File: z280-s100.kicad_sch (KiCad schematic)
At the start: 33 parts, among them J1 S-100 edge connector (100-pin), J2 JTAG header (1x6), J3 Jumper (2-pin header), J4 Jumper (2-pin header), J5 Jumper (2-pin header), J6 Jumper (2-pin header), J7 Jumper (2-pin header), J8 Jumper (2-pin header), U1 Z280 Z-BUS (12 MHz), U10 IS61C5128AS-25 (512Kx8), U11 SST27SF020 (256Kx8), U12 SST27SF020 (256Kx8), U13 MAX232, U14 DS1813, U15 LM7805, U16 74HCT245, U17 74HCT245, U18 74HCT245, U19 74HCT245, U2 ATF1508AS (PLCC-84), U20 74HCT245, U21 74HCT245, U22 IS61C5128AS-25 (512Kx8), U23 IS61C5128AS-25 (512Kx8), U24 ATF1508AS (PLCC-84), U3 74HC573, U4 74HC573, U9 IS61C5128AS-25 (512Kx8), Y1 24 MHz

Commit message: Z280 S-100: 4-layer PCB with power planes and edge-connector test points
gen_pcb.py now emits a 4-layer board (In1.Cu = GND plane, In2.Cu = +5V
plane), imports the S-100 edge connector geometry from the Z80 V3
reference board, and adds a row of test-point vias above each connector
finger. Component reference designators are synced to the schematic's
current annotation (the edge connector is J8). The schematic generator
gained the serial header and symbol text/body layout fixes, and the
schematic, netlist, and PCB were regenerated.

Co-Authored-By: Claude <noreply@anthropic.com>
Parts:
- removed J1: S-100 edge connector (100-pin), Connector_Edge, symbol z280s100:S100_100
- removed J2: JTAG header (1x6), Connector_PinHeader_2.54mm:PinHeader_1x06_P2.54mm_Vertical, symbol z280s100:JTAG
- removed J7, J8: Jumper (2-pin header), Connector_PinHeader_2.54mm:PinHeader_1x02_P2.54mm_Vertical, symbol z280s100:JP
- removed U10, U22, U23: IS61C5128AS-25 (512Kx8), Package_DIP:DIP-32, symbol z280s100:IS61C5128AS
- removed U12: SST27SF020 (256Kx8), Package_DIP:DIP-32, symbol z280s100:SST27SF020
- removed U13: MAX232, Package_DIP:DIP-16, symbol z280s100:MAX232
- removed U14: DS1813, Package_TO_SOT:TO-92, symbol z280s100:DS1813
- removed U15: LM7805, Package_TO_SOT:TO-220-3, symbol z280s100:LM7805
- removed U2: ATF1508AS (PLCC-84), Package_LCC:PLCC-84_THT-Socket, symbol z280s100:ATF1508
- removed U21: 74HCT245, Package_DIP:DIP-20, symbol z280s100:74HCT245
- removed U24: ATF1508AS (PLCC-84), Package_LCC:PLCC-84_THT-Socket, symbol z280s100:ATF1508B
- removed U4: 74HC573, Package_DIP:DIP-20, symbol z280s100:74HC573
- added J1, J2: Jumper (2-pin header), Connector_PinHeader_2.54mm:PinHeader_1x02_P2.54mm_Vertical, symbol z280s100:JP
- added J7: Serial header (2x5), Connector_PinHeader_2.54mm:PinHeader_2x05_P2.54mm_Vertical, symbol z280s100:SERIAL
- added J8: S-100 edge connector (100-pin), Connector_Edge, symbol z280s100:S100_100
- added J9: JTAG header (1x6), Connector_PinHeader_2.54mm:PinHeader_1x06_P2.54mm_Vertical, symbol z280s100:JTAG
- added U10: SST27SF020 (256Kx8), Package_DIP:DIP-32_W15.24mm, symbol z280s100:SST27SF020
- added U12: LM7805, Package_TO_SOT_THT:TO-3, symbol z280s100:LM7805
- added U13: DS1813, Package_TO_SOT:TO-92, symbol z280s100:DS1813
- added U14: MAX232, Package_DIP:DIP-16_W7.62mm, symbol z280s100:MAX232
- added U15: 74HCT245, Package_DIP:DIP-20_W7.62mm, symbol z280s100:74HCT245
- added U2: 74HC573, Package_DIP:DIP-20, symbol z280s100:74HC573
- added U4: ATF1508AS (PLCC-84), Package_LCC:PLCC-84_THT-Socket, symbol z280s100:ATF1508
- added U5: ATF1508AS (PLCC-84), Package_LCC:PLCC-84_THT-Socket, symbol z280s100:ATF1508B
- added U6, U7, U8: IS61C5128AS-25 (512Kx8), Package_DIP:DIP-32_W15.24mm, symbol z280s100:IS61C5128AS
- U11, U9: footprint Package_DIP:DIP-32 -> Package_DIP:DIP-32_W15.24mm
- U16, U17, U18, U19, U20, U3: footprint Package_DIP:DIP-20 -> Package_DIP:DIP-20_W7.62mm
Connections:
- net +16V: now also J8.2 (+16V)
- net +5V: now also J5.2 (B), J6.2 (B), U20.1 (DIR), J1.2 (B), J9.6 (VCC), U12.3 (OUT), U13.3 (VCC), U14.16 (VCC), U15.20 (VCC), U2.20 (VCC), U4.13 (VCCIO), U4.26 (VCCIO), U4.3 (VCCINT), U4.38 (VCCIO), U4.43 (VCCINT), U4.53 (VCCIO), U4.66 (VCCIO), U4.78 (VCCIO), U5.13 (VCCIO), U5.26 (VCCIO), U5.3 (VCCINT), U5.38 (VCCIO), U5.43 (VCCINT), U5.53 (VCCIO), U5.66 (VCCIO), U5.78 (VCCIO), U6.28 (VCC), U7.28 (VCC), U8.28 (VCC); no longer J3.2 (B)
- net +8V: now also J8.1 (+8V), J8.51 (+8V), U12.1 (IN)
- net -16V: now also J8.52 (-16V)
- net A16: now also U17.2 (A0), J2.2 (B), U5.2 (A16), U6.32 (A15), U7.32 (A15), U8.32 (A15); no longer J4.2 (B), U18.2 (A0)
- net A17: now also J3.2 (B), U17.3 (A1), U5.4 (A17), U6.31 (A16), U7.31 (A16), U8.31 (A16); no longer J5.2 (B), U18.3 (A1)
- net A18: now also J4.2 (B), U17.4 (A2), U5.5 (A18), U6.30 (A17), U7.30 (A17), U8.30 (A17); no longer J6.2 (B), U18.4 (A2)
- net A19: now also U17.5 (A3), U5.6 (A19), U6.29 (A18), U7.29 (A18), U8.29 (A18); no longer U18.5 (A3)
- net A20: now also U17.6 (A4), U5.8 (A20); no longer U18.6 (A4)
- net A21: now also U17.7 (A5), U5.9 (A21); no longer U18.7 (A5)
- net A22: now also U17.8 (A6), U5.10 (A22); no longer U18.8 (A6)
- net A23: now also U17.9 (A7), U5.11 (A23); no longer U18.9 (A7)
- net AD0: now also U11.13 (DQ0), U9.11 (DQ0), U2.2 (D0), U5.28 (AD0), U7.11 (DQ0); no longer U3.2 (D0)
- net AD1: now also U11.14 (DQ1), U9.12 (DQ1), U2.3 (D1), U5.29 (AD1), U7.12 (DQ1); no longer U3.3 (D1)
- net AD10: now also U3.4 (D2), U10.15 (DQ2), U5.40 (AD10), U6.13 (DQ2), U8.13 (DQ2); no longer U11.15 (DQ2), U9.13 (DQ2)
- net AD11: now also U3.5 (D3), U10.17 (DQ3), U5.41 (AD11), U6.15 (DQ3), U8.15 (DQ3); no longer U11.17 (DQ3), U9.15 (DQ3)
- net AD12: now also U3.6 (D4), U10.18 (DQ4), U5.44 (AD12), U6.16 (DQ4), U8.16 (DQ4); no longer U11.18 (DQ4), U9.16 (DQ4)
- net AD13: now also U3.7 (D5), U10.19 (DQ5), U5.45 (AD13), U6.17 (DQ5), U8.17 (DQ5); no longer U11.19 (DQ5), U9.17 (DQ5)
- net AD14: now also U3.8 (D6), U10.20 (DQ6), U5.46 (AD14), U6.18 (DQ6), U8.18 (DQ6); no longer U11.20 (DQ6), U9.18 (DQ6)
- net AD15: now also U3.9 (D7), U10.21 (DQ7), U5.48 (AD15), U6.19 (DQ7), U8.19 (DQ7); no longer U11.21 (DQ7), U9.19 (DQ7)
- net AD2: now also U11.15 (DQ2), U9.13 (DQ2), U2.4 (D2), U5.30 (AD2), U7.13 (DQ2); no longer U3.4 (D2)
- net AD3: now also U11.17 (DQ3), U9.15 (DQ3), U2.5 (D3), U5.31 (AD3), U7.15 (DQ3); no longer U3.5 (D3)
- net AD4: now also U11.18 (DQ4), U9.16 (DQ4), U2.6 (D4), U5.33 (AD4), U7.16 (DQ4); no longer U3.6 (D4)
- net AD5: now also U11.19 (DQ5), U9.17 (DQ5), U2.7 (D5), U5.34 (AD5), U7.17 (DQ5); no longer U3.7 (D5)
- net AD6: now also U11.20 (DQ6), U9.18 (DQ6), U2.8 (D6), U5.35 (AD6), U7.18 (DQ6); no longer U3.8 (D6)
- net AD7: now also U11.21 (DQ7), U9.19 (DQ7), U2.9 (D7), U5.36 (AD7), U7.19 (DQ7); no longer U3.9 (D7)
- net AD8: now also U3.2 (D0), U10.13 (DQ0), U5.37 (AD8), U6.11 (DQ0), U8.11 (DQ0); no longer U11.13 (DQ0), U9.11 (DQ0)
- net AD9: now also U3.3 (D1), U10.14 (DQ1), U5.39 (AD9), U6.12 (DQ1), U8.12 (DQ1); no longer U11.14 (DQ1), U9.12 (DQ1)
- net BANK: now also U4.33 (BANK), U5.73 (BANK)
- net BYTE_SEL: now also U15.2 (A0), U4.73 (BYTE_SEL), U5.16 (BYTE_SEL); no longer U16.2 (A0)
- net CPLD_pDBIN: now also U19.4 (A2), U4.51 (CPLD_pDBIN); no longer U20.4 (A2)
- net CPLD_pHLDA: now also U20.2 (A0), U4.54 (CPLD_pHLDA)
- net CPLD_pSTVAL: now also U19.3 (A1), U4.50 (CPLD_pSTVAL); no longer U20.3 (A1)
- net CPLD_pSYNC: now also U19.2 (A0), U4.49 (CPLD_pSYNC); no longer U20.2 (A0)
- net CPLD_pWR: now also U19.5 (A3), U4.52 (CPLD_pWR); no longer U20.5 (A3)
- net CPLD_sHLTA: now also U18.7 (A5), U4.46 (CPLD_sHLTA); no longer U19.7 (A5)
- net CPLD_sINP: now also U18.4 (A2), U4.41 (CPLD_sINP); no longer U19.4 (A2)
- net CPLD_sINTA: now also U18.6 (A4), U4.45 (CPLD_sINTA); no longer U19.6 (A4)
- net CPLD_sMEMR: now also U18.2 (A0), U4.39 (CPLD_sMEMR); no longer U19.2 (A0)
- net CPLD_sOUT: now also U18.5 (A3), U4.44 (CPLD_sOUT); no longer U19.5 (A3)
- net CPLD_sWO: now also U18.3 (A1), U4.40 (CPLD_sWO); no longer U19.3 (A1)
- net CPLD_sXTRQ: now also U18.8 (A6), U4.48 (CPLD_sXTRQ); no longer U19.8 (A6)
- net FLASH_A15: now also J2.1 (A), U10.3 (A15); no longer J4.1 (A)
- net FLASH_A16: now also J3.1 (A), U10.2 (A16); no longer J5.1 (A)
- net FLASH_A17: now also J4.1 (A), U10.30 (A17); no longer J6.1 (A)
- net FLASH_CE: now also U10.22 (CE), U4.61 (FLASH_CE)
- net FLASH_OE: now also U10.24 (OE), U4.63 (FLASH_OE)
- net FLASH_PGM: now also J5.1 (A), U10.31 (PGM)
- net FLASH_VDD: now also J6.1 (A), U10.32 (VCC)
- net FLASH_VPP: now also J1.1 (A), U10.1 (VPP); no longer J3.1 (A)
- net FLASH_WIN: now also U4.31 (FLASH_WIN), U5.70 (FLASH_WIN)
- net GND: now also U20.19 (OE), U20.3 (A1), U20.4 (A2), U20.5 (A3), U20.6 (A4), U20.7 (A5), U20.8 (A6), U20.9 (A7), J7.10 (GND), J7.3 (GND), J7.4 (GND), J7.5 (GND), J7.6 (GND), J7.7 (GND), J7.8 (GND), J7.9 (GND), J8.100 (GND), J8.20 (GND), J8.50 (GND), J8.53 (GND), J8.70 (GND), J9.5 (GND), U10.16 (GND), U12.2 (GND), U13.1 (GND), U14.15 (GND), U15.10 (GND), U2.1 (OE), U2.10 (GND), U4.19 (GND), U4.32 (GND), U4.42 (GND), U4.47 (GND), U4.59 (GND), U4.7 (GND), U4.72 (GND), U4.82 (GND), U5.19 (GND), U5.32 (GND), U5.42 (GND), U5.47 (GND), U5.59 (GND), U5.7 (GND), U5.72 (GND), U5.82 (GND), U6.14 (GND), U7.14 (GND), U8.14 (GND)
- net JTAG_CHAIN: now also U4.71 (TDO), U5.14 (TDI)
- net JTAG_TCK: now also J9.1 (TCK), U4.62 (TCK), U5.62 (TCK)
- net JTAG_TDI: now also J9.3 (TDI), U4.14 (TDI)
- net JTAG_TDO: now also J9.4 (TDO), U5.71 (TDO)
- net JTAG_TMS: now also J9.2 (TMS), U4.23 (TMS), U5.23 (TMS)
- net LA0: now also U2.12 (Q0), U4.27 (LA0); no longer U3.12 (Q0)
- net LA1: now also U10.12 (A0), U15.3 (A1), U2.13 (Q1), U4.28 (LA1); no longer U16.3 (A1), U3.13 (Q1)
- net LA10: now also U16.4 (A2), U3.14 (Q2), U10.26 (A9), U6.24 (A9), U7.24 (A9), U8.24 (A9); no longer U17.4 (A2)
- net LA11: now also U16.5 (A3), U3.15 (Q3), U10.23 (A10), U6.21 (A10), U7.21 (A10), U8.21 (A10); no longer U17.5 (A3)
- net LA12: now also U16.6 (A4), U3.16 (Q4), U10.25 (A11), U6.23 (A11), U7.23 (A11), U8.23 (A11); no longer U17.6 (A4)
- net LA13: now also U16.7 (A5), U3.17 (Q5), U10.4 (A12), U6.2 (A12), U7.2 (A12), U8.2 (A12); no longer U17.7 (A5)
- net LA14: now also U16.8 (A6), U3.18 (Q6), U10.28 (A13), U6.26 (A13), U7.26 (A13), U8.26 (A13); no longer U17.8 (A6)
- net LA15: now also U16.9 (A7), U3.19 (Q7), U10.29 (A14), U6.1 (A14), U7.1 (A14), U8.1 (A14); no longer U17.9 (A7)
- net LA2: now also U10.11 (A1), U15.4 (A2), U2.14 (Q2), U4.29 (LA2); no longer U16.4 (A2), U3.14 (Q2)
- net LA3: now also U10.10 (A2), U15.5 (A3), U2.15 (Q3), U6.8 (A2), U7.8 (A2), U8.8 (A2); no longer U16.5 (A3), U3.15 (Q3)
- net LA4: now also U10.9 (A3), U15.6 (A4), U2.16 (Q4), U6.7 (A3), U7.7 (A3), U8.7 (A3); no longer U16.6 (A4), U3.16 (Q4)
- net LA5: now also U10.8 (A4), U15.7 (A5), U2.17 (Q5), U6.6 (A4), U7.6 (A4), U8.6 (A4); no longer U16.7 (A5), U3.17 (Q5)
- net LA6: now also U10.7 (A5), U15.8 (A6), U2.18 (Q6), U6.5 (A5), U7.5 (A5), U8.5 (A5); no longer U16.8 (A6), U3.18 (Q6)
- net LA7: now also U10.6 (A6), U15.9 (A7), U2.19 (Q7), U6.4 (A6), U7.4 (A6), U8.4 (A6); no longer U16.9 (A7), U3.19 (Q7)
- net LA8: now also U16.2 (A0), U3.12 (Q0), U10.5 (A7), U6.3 (A7), U7.3 (A7), U8.3 (A7); no longer U17.2 (A0)
- net LA9: now also U16.3 (A1), U3.13 (Q1), U10.27 (A8), U6.25 (A8), U7.25 (A8), U8.25 (A8); no longer U17.3 (A1)
- net LATCH_LE: now also U2.11 (LE), U4.64 (LATCH_LE)
- net MASTER_ACTIVE: now also U4.69 (MASTER_ACTIVE), U5.12 (MASTER_ACTIVE)
- net MASTER_WRITE: now also U4.70 (MASTER_WRITE), U5.15 (MASTER_WRITE)
- net MAX_C1M: now also U14.3 (C1-)
- net MAX_C1P: now also U14.1 (C1+)
- net MAX_C2M: now also U14.5 (C2-)
- net MAX_C2P: now also U14.4 (C2+)
- net MAX_RS232_TX: now also J7.1 (RS232_TX), U14.14 (T1OUT)
- net MAX_VM: now also U14.6 (V-)
- net MAX_VP: now also U14.2 (V+)
- net MEM_CE0: now also U4.55 (MEM_CE0), U6.20 (CE), U7.20 (CE); no longer U9.20 (CE)
- net MEM_CE1: now also U9.20 (CE), U4.56 (MEM_CE1), U8.20 (CE)
- net MEM_OE: now also U4.57 (MEM_OE), U6.22 (OE), U7.22 (OE), U8.22 (OE)
- net MEM_WE_H: now also U9.27 (WE), U4.60 (MEM_WE_H), U7.27 (WE)
- net MEM_WE_L: now also U4.58 (MEM_WE_L), U6.27 (WE), U8.27 (WE); no longer U9.27 (WE)
- net NC: now also U14.10 (T2IN), U14.7 (T2OUT), U14.8 (R2IN), U14.9 (R2OUT)
- net S100_A0: now also J8.79 (A0), U15.11 (B0); no longer U16.11 (B0)
- net S100_A1: now also J8.80 (A1), U15.12 (B1); no longer U16.12 (B1)
- net S100_A10: now also U16.13 (B2), J8.37 (A10); no longer U17.13 (B2)
- net S100_A11: now also U16.14 (B3), J8.87 (A11); no longer U17.14 (B3)
- net S100_A12: now also U16.15 (B4), J8.33 (A12); no longer U17.15 (B4)
- net S100_A13: now also U16.16 (B5), J8.85 (A13); no longer U17.16 (B5)
- net S100_A14: now also U16.17 (B6), J8.86 (A14); no longer U17.17 (B6)
- net S100_A15: now also U16.18 (B7), J8.32 (A15); no longer U17.18 (B7)
- net S100_A16: now also U17.11 (B0), J8.16 (A16); no longer U18.11 (B0)
- net S100_A17: now also U17.12 (B1), J8.17 (A17); no longer U18.12 (B1)
- net S100_A18: now also U17.13 (B2), J8.15 (A18); no longer U18.13 (B2)
- net S100_A19: now also U17.14 (B3), J8.59 (A19); no longer U18.14 (B3)
- net S100_A2: now also J8.81 (A2), U15.13 (B2); no longer U16.13 (B2)
- net S100_A20: now also U17.15 (B4), J8.61 (A20); no longer U18.15 (B4)
- net S100_A21: now also U17.16 (B5), J8.62 (A21); no longer U18.16 (B5)
- net S100_A22: now also U17.17 (B6), J8.63 (A22); no longer U18.17 (B6)
- net S100_A23: now also U17.18 (B7), J8.64 (A23); no longer U18.18 (B7)
- net S100_A3: now also J8.31 (A3), U15.14 (B3); no longer U16.14 (B3)
- net S100_A4: now also J8.30 (A4), U15.15 (B4); no longer U16.15 (B4)
- net S100_A5: now also J8.29 (A5), U15.16 (B5); no longer U16.16 (B5)
- net S100_A6: now also J8.82 (A6), U15.17 (B6); no longer U16.17 (B6)
- net S100_A7: now also J8.83 (A7), U15.18 (B7); no longer U16.18 (B7)
- net S100_A8: now also U16.11 (B0), J8.84 (A8); no longer U17.11 (B0)
- net S100_A9: now also U16.12 (B1), J8.34 (A9); no longer U17.12 (B1)
- net S100_ADSB: now also J8.22 (ADSB), U5.22 (S100_ADSB)
- net S100_A_DIR: now also U15.1 (DIR), U5.75 (S100_A_DIR); no longer U18.1 (DIR)
- net S100_A_OE: now also U15.19 (OE), U5.74 (S100_A_OE); no longer U18.19 (OE)
- net S100_CDSB: now also J8.19 (CDSB), U5.27 (S100_CDSB)
- net S100_CLOCK: now also J8.49 (CLOCK)
- net S100_C_OE: now also U19.19 (OE), U5.77 (S100_C_OE); no longer U20.19 (OE)
- net S100_DI0: now also J8.95 (DI0), U5.58 (S100_DI0)
- net S100_DI1: now also J8.94 (DI1), U5.60 (S100_DI1)
- net S100_DI2: now also J8.41 (DI2), U5.61 (S100_DI2)
- net S100_DI3: now also J8.42 (DI3), U5.63 (S100_DI3)
- net S100_DI4: now also J8.91 (DI4), U5.64 (S100_DI4)
- net S100_DI5: now also J8.92 (DI5), U5.65 (S100_DI5)
- net S100_DI6: now also J8.93 (DI6), U5.67 (S100_DI6)
- net S100_DI7: now also J8.43 (DI7), U5.68 (S100_DI7)
- net S100_DMA0: now also J8.55 (DMA0)
- net S100_DMA1: now also J8.56 (DMA1)
- net S100_DMA2: now also J8.57 (DMA2)
- net S100_DMA3: now also J8.14 (DMA3)
- net S100_DO0: now also J8.36 (DO0), U5.49 (S100_DO0)
- net S100_DO1: now also J8.35 (DO1), U5.50 (S100_DO1)
- net S100_DO2: now also J8.88 (DO2), U5.51 (S100_DO2)
- net S100_DO3: now also J8.89 (DO3), U5.52 (S100_DO3)
- net S100_DO4: now also J8.38 (DO4), U5.54 (S100_DO4)
- net S100_DO5: now also J8.39 (DO5), U5.55 (S100_DO5)
- net S100_DO6: now also J8.40 (DO6), U5.56 (S100_DO6)
- net S100_DO7: now also J8.90 (DO7), U5.57 (S100_DO7)
- net S100_DODSB: now also J8.23 (DODSB), U5.24 (S100_DODSB)
- net S100_ERROR: now also J8.98 (ERROR)
- net S100_HOLD: now also J8.74 (HOLD), U4.20 (S100_HOLD)
- net S100_INT: now also J8.73 (INT), U4.17 (S100_INT)
- net S100_MWRT: now also J8.68 (MWRT)
- net S100_NMI: now also J8.12 (NMI), U4.18 (S100_NMI)
- net S100_PHANTOM: now also J8.67 (PHANTOM)
- net S100_PHI: now also J8.24 (PHI)
- net S100_POC: now also J8.99 (POC)
- net S100_PWRFAIL: now also J8.13 (PWRFAIL)
- net S100_RESET: now also J8.75 (RESET)
- net S100_SC_DIR: now also U18.1 (DIR), U5.79 (S100_SC_DIR); no longer U20.1 (DIR)
- net S100_SDSB: now also J8.18 (SDSB), U5.25 (S100_SDSB)
- net S100_SIXTN: now also J8.60 (SIXTN), U4.24 (S100_SIXTN), U5.83 (S100_SIXTN)
- net S100_SLAVE_CLR: now also J8.54 (SLAVE_CLR)
- net S100_S_OE: now also U18.19 (OE), U5.76 (S100_S_OE); no longer U19.19 (OE)
- net S100_VI0: now also J8.4 (VI0)
- net S100_VI1: now also J8.5 (VI1)
- net S100_VI2: now also J8.6 (VI2)
- net S100_VI3: now also J8.7 (VI3)
- net S100_VI4: now also J8.8 (VI4)
- net S100_VI5: now also J8.9 (VI5)
- net S100_VI6: now also J8.10 (VI6)
- net S100_VI7: now also J8.11 (VI7)
- net S100_XRDY: now also J8.3 (XRDY), U4.22 (S100_XRDY), U5.81 (S100_XRDY)
- net S100_pDBIN: now also U19.13 (B2), J8.78 (pDBIN); no longer U20.13 (B2)
- net S100_pHLDA: now also U20.11 (B0), J8.26 (pHLDA)
- net S100_pRDY: now also J8.72 (pRDY), U4.21 (S100_pRDY), U5.80 (S100_pRDY)
- net S100_pSTVAL: now also U19.12 (B1), J8.25 (pSTVAL); no longer U20.12 (B1)
- net S100_pSYNC: now also U19.11 (B0), J8.76 (pSYNC); no longer U20.11 (B0)
- net S100_pWR: now also U19.14 (B3), J8.77 (pWR); no longer U20.14 (B3)
- net S100_sHLTA: now also U18.16 (B5), J8.48 (sHLTA); no longer U19.16 (B5)
- net S100_sINP: now also U18.13 (B2), J8.46 (sINP); no longer U19.13 (B2)
- net S100_sINTA: now also U18.15 (B4), J8.96 (sINTA); no longer U19.15 (B4)
- net S100_sM1: now also J8.44 (sM1)
- net S100_sMEMR: now also U18.11 (B0), J8.47 (sMEMR), U5.18 (S100_sMEMR); no longer U19.11 (B0)
- net S100_sOUT: now also U18.14 (B3), J8.45 (sOUT); no longer U19.14 (B3)
- net S100_sWO: now also U18.12 (B1), J8.97 (sWO), U5.20 (S100_sWO); no longer U19.12 (B1)
- net S100_sXTRQ: now also U18.17 (B6), J8.58 (sXTRQ), U5.21 (S100_sXTRQ); no longer U19.17 (B6)
- net SLAVE: now also U4.68 (SLAVE), U5.1 (SLAVE)
- net SLAVE_ONLY: now also U4.25 (SLAVE_ONLY)
- net SRAM_A0: now also U4.65 (SRAM_A0), U6.10 (A0), U7.10 (A0), U8.10 (A0)
- net SRAM_A1: now also U4.67 (SRAM_A1), U6.9 (A1), U7.9 (A1), U8.9 (A1)
- net SRAM_WIN: now also U4.30 (SRAM_WIN), U5.69 (SRAM_WIN)
- net XFR16: now also U4.74 (XFR16), U5.17 (XFR16)
- net Z_AS: now also U4.1 (Z_AS)
- net Z_BUSACK: now also U4.15 (Z_BUSACK)
- net Z_BUSREQ: now also U4.37 (Z_BUSREQ)
- net Z_BW: now also U4.5 (Z_BW)
- net Z_CLK: now also U4.83 (Z_CLK_IN)
- net Z_DS: now also U4.2 (Z_DS)
- net Z_IE: now also U4.11 (Z_IE)
- net Z_INT: now also U4.35 (Z_INT)
- net Z_NMI: now also U4.36 (Z_NMI)
- net Z_OE: now also U4.12 (Z_OE)
- net Z_RESET: now also U13.2 (RST), U4.16 (Z_RESET)
- net Z_RW: now also U4.4 (Z_RW)
- net Z_RXD: now also U14.12 (R1OUT)
- net Z_ST0: now also U4.6 (Z_ST0)
- net Z_ST1: now also U4.8 (Z_ST1)
- net Z_ST2: now also U4.9 (Z_ST2)
- net Z_ST3: now also U4.10 (Z_ST3)
- net Z_TXD: now also U14.11 (T1IN)
- net Z_WAIT: now also U4.34 (Z_WAIT)
- new net MAX_RS232_RX: J7.2 (RS232_RX), U14.13 (R1IN)

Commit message: Z280 S-100: re-partition CPLDs, external decode, reset/BTI config
Split the two ATF1508s by function: z280-s100-ad.pld (data path) owns
AD0-15 demux/burst/byte-mux, z280-s100-ctl.pld (decider) owns the FSM,
arbitration, memory control and steering. Replace the old
control.pld/data.pld pair.

Move A16-23 decode off-chip to a 74F138 + two 74F521s (SRAM/FLASH/slave
window); drop the 74HC573 latches. Boot ROM is now 2x AT28C256 (word-wide
fetch needs two parts).

Add reset/BTI loading: a 74HCT244 tri-state driver (CFG_OE-gated) drives
AD0-7 during reset, config jumpers J10-J17 strap the BTI value, and a
15-clock hold counter keeps WAIT asserted past reset. Fix dedicated pins
(GCLR/OE1/OE2 tied inactive) and make SIXTN bidirectional.

PCB: RAM/ROM clustered left, decode + BTI + config straps top-right,
data CPLD aligned above the memory column.

Co-Authored-By: Claude <noreply@anthropic.com>
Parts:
- removed J1, J2, J3, J4, J5, J6: Jumper (2-pin header), Connector_PinHeader_2.54mm:PinHeader_1x02_P2.54mm_Vertical, symbol z280s100:JP
- removed U10, U11: SST27SF020 (256Kx8), Package_DIP:DIP-32_W15.24mm, symbol z280s100:SST27SF020
- removed U2: 74HC573, Package_DIP:DIP-20, symbol z280s100:74HC573
- removed U3: 74HC573, Package_DIP:DIP-20_W7.62mm, symbol z280s100:74HC573
- added J10, J11, J12, J13, J14, J15, J16, J17: Jumper (3-pin header), Connector_PinHeader_2.54mm:PinHeader_1x03_P2.54mm_Vertical, symbol z280s100:JP3
- added U10, U11: AT28C256 (32Kx8), Package_DIP:DIP-28_W15.24mm, symbol z280s100:AT28C256
- added U21: 74HCT244, Package_DIP:DIP-20, symbol z280s100:74HCT244
- added U22: 74F138, Package_DIP:DIP-16, symbol z280s100:74F138
- added U23, U24: 74F521, Package_DIP:DIP-20, symbol z280s100:74F521
- U12: footprint Package_TO_SOT_THT:TO-3 -> Package_TO_SOT:TO-220-3
- U14: footprint Package_DIP:DIP-16_W7.62mm -> Package_DIP:DIP-16
- U15, U16, U17, U18, U19, U20: footprint Package_DIP:DIP-20_W7.62mm -> Package_DIP:DIP-20
- U6, U7, U8, U9: footprint Package_DIP:DIP-32_W15.24mm -> Package_DIP:DIP-32
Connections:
- net LATCH_LE is gone; now on net S100_A_OE: U4.64 (S100_A_OE)
- net +5V: now also U4.1 (GCLR), U4.2 (OE2), U4.84 (OE1), U5.1 (GCLR), U5.2 (OE2), U5.84 (OE1), J10.1 (HIGH), J11.1 (HIGH), J12.1 (HIGH), J13.1 (HIGH), J14.1 (HIGH), J15.1 (HIGH), J16.1 (HIGH), J17.1 (HIGH), U10.28 (VCC), U11.28 (VCC), U21.20 (+5V), U22.16 (+5V), U22.6 (G1), U23.12 (P4), U23.14 (P5), U23.16 (P6), U23.18 (P7), U23.20 (+5V), U24.20 (+5V)
- net A16: now also U23.3 (Q0), U24.2 (P0), U24.3 (Q0); no longer U5.2 (A16)
- net A17: now also U23.5 (Q1), U24.4 (P1), U24.5 (Q1); no longer U5.4 (A17)
- net A18: now also U23.7 (Q2), U24.6 (P2), U24.7 (Q2); no longer U5.5 (A18)
- net A19: now also U23.9 (Q3), U24.8 (P3), U24.9 (Q3); no longer U5.6 (A19)
- net A20: now also U23.11 (Q4), U24.11 (Q4), U24.12 (P4); no longer U5.8 (A20)
- net A21: now also U22.1 (A0), U23.13 (Q5), U24.13 (Q5); no longer U5.9 (A21)
- net A22: now also U22.2 (A1), U23.15 (Q6), U24.15 (Q6); no longer U5.10 (A22)
- net A23: now also U22.3 (A2), U23.17 (Q7), U24.17 (Q7); no longer U5.11 (A23)
- net AD0: now also U5.40 (AD0), U11.11 (DQ0), U21.18 (Y0); no longer U5.28 (AD0)
- net AD1: now also U5.41 (AD1), U11.12 (DQ1), U21.16 (Y1); no longer U5.29 (AD1)
- net AD10: now also U5.54 (AD10), U10.13 (DQ2); no longer U5.40 (AD10)
- net AD11: now also U5.55 (AD11), U10.15 (DQ3); no longer U5.41 (AD11)
- net AD12: now also U5.56 (AD12), U10.16 (DQ4); no longer U5.44 (AD12)
- net AD13: now also U5.57 (AD13), U10.17 (DQ5); no longer U5.45 (AD13)
- net AD14: now also U5.58 (AD14), U10.18 (DQ6); no longer U5.46 (AD14)
- net AD15: now also U5.60 (AD15), U10.19 (DQ7); no longer U5.48 (AD15)
- net AD2: now also U5.44 (AD2), U11.13 (DQ2), U21.14 (Y2); no longer U5.30 (AD2)
- net AD3: now also U5.45 (AD3), U11.15 (DQ3), U21.12 (Y3); no longer U5.31 (AD3)
- net AD4: now also U5.46 (AD4), U11.16 (DQ4), U21.9 (Y4); no longer U5.33 (AD4)
- net AD5: now also U5.48 (AD5), U11.17 (DQ5), U21.7 (Y5); no longer U5.34 (AD5)
- net AD6: now also U5.49 (AD6), U11.18 (DQ6), U21.5 (Y6); no longer U5.35 (AD6)
- net AD7: now also U5.50 (AD7), U11.19 (DQ7), U21.3 (Y7); no longer U5.36 (AD7)
- net AD8: now also U5.51 (AD8), U10.11 (DQ0); no longer U5.37 (AD8)
- net AD9: now also U5.52 (AD9), U10.12 (DQ1); no longer U5.39 (AD9)
- net BANK: no longer U5.73 (BANK)
- net FLASH_CE: now also U10.20 (CE), U11.20 (CE)
- net FLASH_OE: now also U10.22 (OE), U11.22 (OE)
- net FLASH_WIN: now also U23.19 (PEQQ); no longer U5.70 (FLASH_WIN)
- net GND: now also J10.3 (LOW), J11.3 (LOW), J12.3 (LOW), J13.3 (LOW), J14.3 (LOW), J15.3 (LOW), J16.3 (LOW), J17.3 (LOW), U10.14 (GND), U11.14 (GND), U21.10 (GND), U22.4 (G2A), U22.5 (G2B), U22.8 (GND), U23.1 (G), U23.10 (GND), U23.2 (P0), U23.4 (P1), U23.6 (P2), U23.8 (P3), U24.1 (G), U24.10 (GND), U24.14 (P5), U24.16 (P6), U24.18 (P7)
- net LA0: now also U5.18 (LA0)
- net LA1: no longer U4.28 (LA1)
- net LA10: no longer U6.24 (A9), U7.24 (A9), U8.24 (A9), U9.24 (A9)
- net LA11: no longer U6.21 (A10), U7.21 (A10), U8.21 (A10), U9.21 (A10)
- net LA12: no longer U6.23 (A11), U7.23 (A11), U8.23 (A11), U9.23 (A11)
- net LA13: no longer U6.2 (A12), U7.2 (A12), U8.2 (A12), U9.2 (A12)
- net LA14: no longer U6.26 (A13), U7.26 (A13), U8.26 (A13), U9.26 (A13)
- net LA15: no longer U6.1 (A14), U7.1 (A14), U8.1 (A14), U9.1 (A14)
- net LA2: no longer U4.29 (LA2)
- net LA3: no longer U6.8 (A2), U7.8 (A2), U8.8 (A2), U9.8 (A2)
- net LA4: no longer U6.7 (A3), U7.7 (A3), U8.7 (A3), U9.7 (A3)
- net LA5: no longer U6.6 (A4), U7.6 (A4), U8.6 (A4), U9.6 (A4)
- net LA6: no longer U6.5 (A5), U7.5 (A5), U8.5 (A5), U9.5 (A5)
- net LA7: no longer U6.4 (A6), U7.4 (A6), U8.4 (A6), U9.4 (A6)
- net LA8: no longer U6.3 (A7), U7.3 (A7), U8.3 (A7), U9.3 (A7)
- net LA9: no longer U6.25 (A8), U7.25 (A8), U8.25 (A8), U9.25 (A8)
- net S100_ADSB: now also U4.12 (S100_ADSB); no longer U5.22 (S100_ADSB)
- net S100_A_OE: no longer U5.74 (S100_A_OE)
- net S100_CDSB: now also U4.28 (S100_CDSB); no longer U5.27 (S100_CDSB)
- net S100_C_OE: now also U4.67 (S100_C_OE); no longer U5.77 (S100_C_OE)
- net S100_DI0: now also U5.73 (S100_DI0); no longer U5.58 (S100_DI0)
- net S100_DI1: now also U5.74 (S100_DI1); no longer U5.60 (S100_DI1)
- net S100_DI2: now also U5.75 (S100_DI2); no longer U5.61 (S100_DI2)
- net S100_DI3: now also U5.76 (S100_DI3); no longer U5.63 (S100_DI3)
- net S100_DI4: now also U5.77 (S100_DI4); no longer U5.64 (S100_DI4)
- net S100_DI5: now also U5.79 (S100_DI5); no longer U5.65 (S100_DI5)
- net S100_DI6: now also U5.80 (S100_DI6); no longer U5.67 (S100_DI6)
- net S100_DI7: now also U5.81 (S100_DI7); no longer U5.68 (S100_DI7)
- net S100_DO0: now also U5.61 (S100_DO0); no longer U5.49 (S100_DO0)
- net S100_DO1: now also U5.63 (S100_DO1); no longer U5.50 (S100_DO1)
- net S100_DO2: now also U5.64 (S100_DO2); no longer U5.51 (S100_DO2)
- net S100_DO3: now also U5.65 (S100_DO3); no longer U5.52 (S100_DO3)
- net S100_DO4: now also U5.67 (S100_DO4); no longer U5.54 (S100_DO4)
- net S100_DO5: now also U5.68 (S100_DO5); no longer U5.55 (S100_DO5)
- net S100_DO6: now also U5.69 (S100_DO6); no longer U5.56 (S100_DO6)
- net S100_DO7: now also U5.70 (S100_DO7); no longer U5.57 (S100_DO7)
- net S100_DODSB: now also U5.8 (S100_DODSB); no longer U5.24 (S100_DODSB)
- net S100_SDSB: now also U4.25 (S100_SDSB); no longer U5.25 (S100_SDSB)
- net S100_SIXTN: no longer U5.83 (S100_SIXTN)
- net S100_S_OE: now also U4.65 (S100_S_OE); no longer U5.76 (S100_S_OE)
- net S100_XRDY: no longer U5.81 (S100_XRDY)
- net S100_pRDY: no longer U5.80 (S100_pRDY)
- net S100_sMEMR: no longer U5.18 (S100_sMEMR)
- net S100_sWO: no longer U5.20 (S100_sWO)
- net S100_sXTRQ: no longer U5.21 (S100_sXTRQ)
- net SLAVE: now also U5.17 (SLAVE); no longer U5.1 (SLAVE)
- net SLAVE_ONLY: no longer U4.25 (SLAVE_ONLY)
- net SRAM_WIN: now also U22.15 (Y0); no longer U5.69 (SRAM_WIN)
- net XFR16: now also U5.15 (XFR16); no longer U5.17 (XFR16)
- net Z_AS: now also U4.77 (Z_AS), U5.4 (Z_AS); no longer U4.1 (Z_AS)
- net Z_CLK: now also U5.83 (Z_CLK_IN)
- net Z_DS: now also U4.79 (Z_DS), U5.5 (Z_DS); no longer U4.2 (Z_DS)
- net Z_OE: no longer U4.12 (Z_OE)
- net BYTE_SEL renamed SPLIT
- net SPLIT: no longer U15.2 (A0)
- net MASTER_ACTIVE renamed MST_RD
- net MST_RD: now also U5.9 (MST_RD); no longer U5.12 (MASTER_ACTIVE)
- net MASTER_WRITE renamed MST_WR
- net MST_WR: now also U5.10 (MST_WR); no longer U5.15 (MASTER_WRITE)
- net S100_A_DIR renamed S100_DIR
- net S100_DIR: now also U18.1 (DIR), U19.1 (DIR), U5.6 (S100_DIR); no longer U5.75 (S100_A_DIR)
- removed net S100_SC_DIR: U18.1 (DIR), U19.1 (DIR), U5.79 (S100_SC_DIR)
- net SRAM_A0 renamed A1
- net A1: now also U5.21 (A1), U10.10 (A0), U11.10 (A0); no longer U4.65 (SRAM_A0)
- net SRAM_A1 renamed A2
- net A2: now also U5.22 (A2), U10.9 (A1), U11.9 (A1); no longer U4.67 (SRAM_A1)
- new net A0: U15.2 (A0), U5.20 (A0)
- new net A10: U10.24 (A9), U11.24 (A9), U5.33 (A10), U6.24 (A9), U7.24 (A9), U8.24 (A9), U9.24 (A9)
- new net A11: U10.21 (A10), U11.21 (A10), U5.34 (A11), U6.21 (A10), U7.21 (A10), U8.21 (A10), U9.21 (A10)
- new net A12: U10.23 (A11), U11.23 (A11), U5.35 (A12), U6.23 (A11), U7.23 (A11), U8.23 (A11), U9.23 (A11)
- new net A13: U10.2 (A12), U11.2 (A12), U5.36 (A13), U6.2 (A12), U7.2 (A12), U8.2 (A12), U9.2 (A12)
- new net A14: U10.26 (A13), U11.26 (A13), U5.37 (A14), U6.26 (A13), U7.26 (A13), U8.26 (A13), U9.26 (A13)
- new net A15: U10.1 (A14), U11.1 (A14), U5.39 (A15), U6.1 (A14), U7.1 (A14), U8.1 (A14), U9.1 (A14)
- new net A3: U10.8 (A2), U11.8 (A2), U5.24 (A3), U6.8 (A2), U7.8 (A2), U8.8 (A2), U9.8 (A2)
- new net A4: U10.7 (A3), U11.7 (A3), U5.25 (A4), U6.7 (A3), U7.7 (A3), U8.7 (A3), U9.7 (A3)
- new net A5: U10.6 (A4), U11.6 (A4), U5.27 (A5), U6.6 (A4), U7.6 (A4), U8.6 (A4), U9.6 (A4)
- new net A6: U10.5 (A5), U11.5 (A5), U5.28 (A6), U6.5 (A5), U7.5 (A5), U8.5 (A5), U9.5 (A5)
- new net A7: U10.4 (A6), U11.4 (A6), U5.29 (A7), U6.4 (A6), U7.4 (A6), U8.4 (A6), U9.4 (A6)
- new net A8: U10.3 (A7), U11.3 (A7), U5.30 (A8), U6.3 (A7), U7.3 (A7), U8.3 (A7), U9.3 (A7)
- new net A9: U10.25 (A8), U11.25 (A8), U5.31 (A9), U6.25 (A8), U7.25 (A8), U8.25 (A8), U9.25 (A8)
- new net BTI_AD0: J10.2 (SEL), U21.2 (A0)
- new net BTI_AD1: J11.2 (SEL), U21.4 (A1)
- new net BTI_AD2: J12.2 (SEL), U21.6 (A2)
- new net BTI_AD3: J13.2 (SEL), U21.8 (A3)
- new net BTI_AD4: J14.2 (SEL), U21.11 (A4)
- new net BTI_AD5: J15.2 (SEL), U21.13 (A5)
- new net BTI_AD6: J16.2 (SEL), U21.15 (A6)
- new net BTI_AD7: J17.2 (SEL), U21.17 (A7)
- new net CFG_OE: U21.1 (OE1), U21.19 (OE2), U4.75 (CFG_OE)
- new net FLASH_WE: U10.27 (WE), U11.27 (WE), U4.76 (FLASH_WE)
- new net SLAVE_WIN: U24.19 (PEQQ), U4.29 (SLAVE_WIN)
- new net SLV_RD: U4.80 (SLV_RD), U5.11 (SLV_RD)
- new net SLV_WR: U4.81 (SLV_WR), U5.12 (SLV_WR)

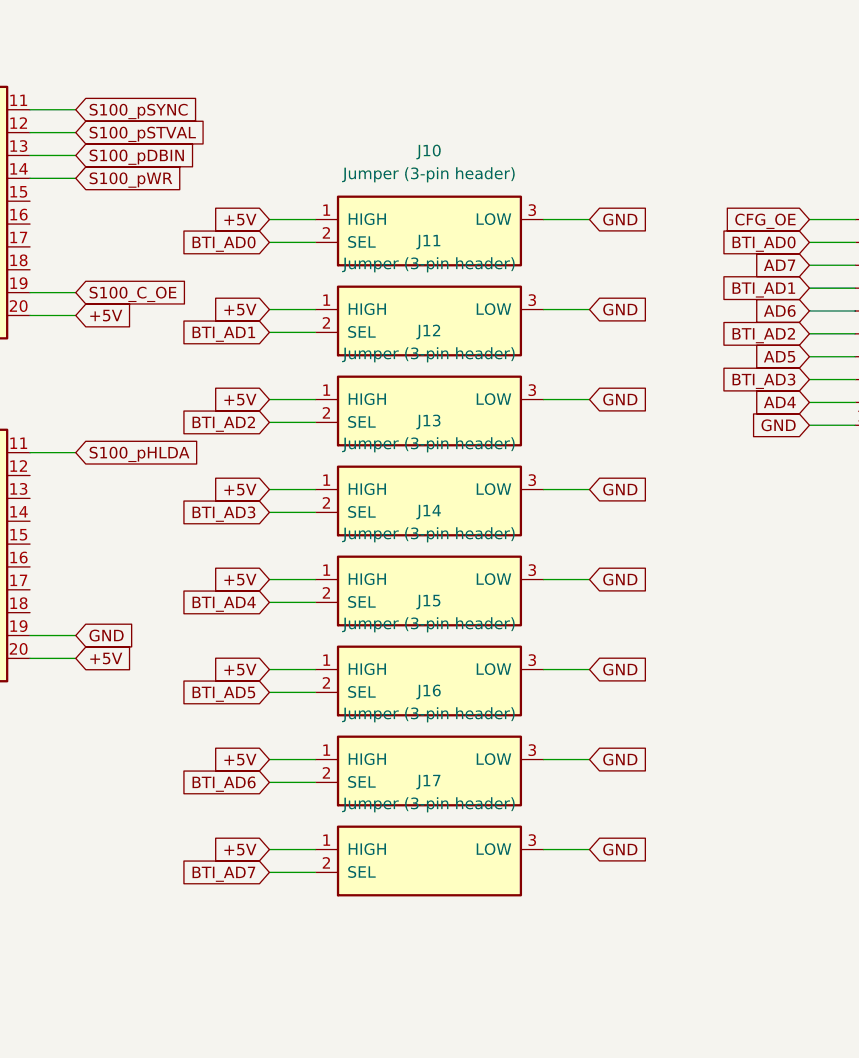
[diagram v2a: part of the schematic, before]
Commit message: Config straps: consolidate 8x 3-pin jumpers into one 3x8 header
Replace J10-J17 (eight PinHeader_1x03) with a single 24-pin 3x8 header
(J10): one row per BTI bit, col 0 = +5V, col 1 = BTI_ADn, col 2 = GND.
Adds a JP3x8 schematic symbol and a hdr_3x8_fp PCB footprint (pin 1
top-left, row-major, matching the symbol), regenerates the netlist and
board. DRC clean (0 shorting items).

Co-Authored-By: Claude <noreply@anthropic.com>
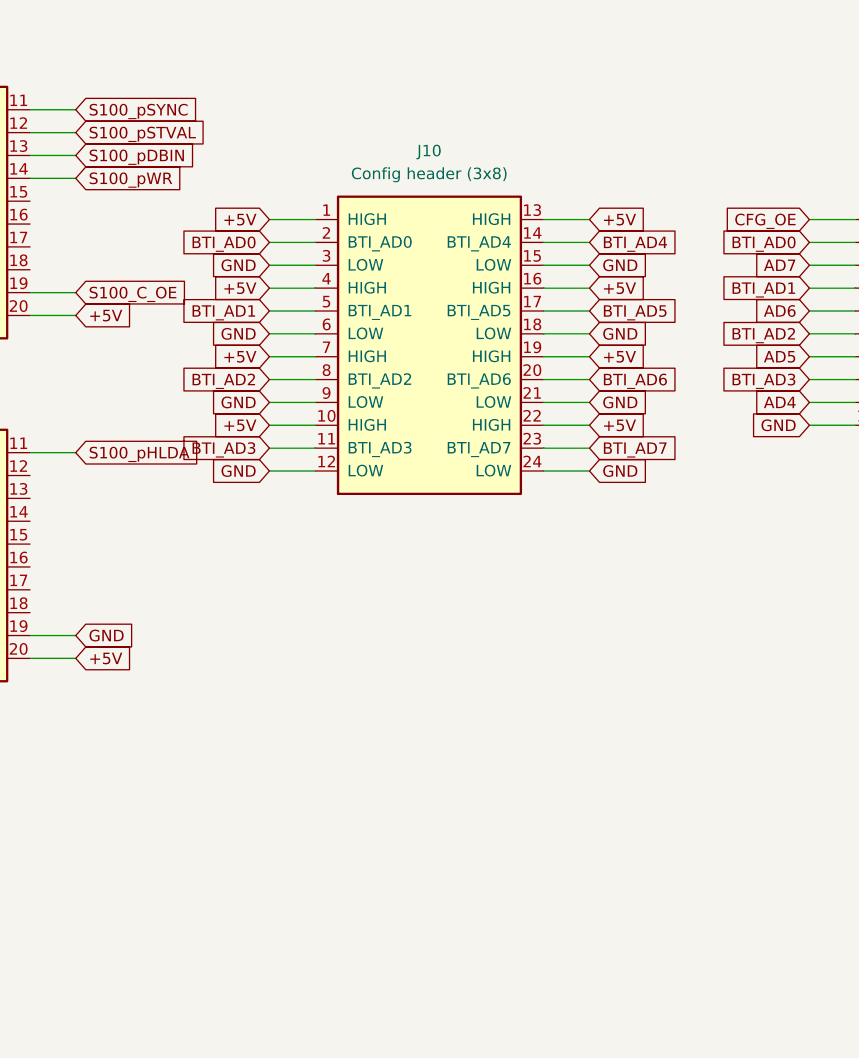
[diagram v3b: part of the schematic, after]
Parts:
- removed J10, J11, J12, J13, J14, J15, J16, J17: Jumper (3-pin header), Connector_PinHeader_2.54mm:PinHeader_1x03_P2.54mm_Vertical, symbol z280s100:JP3
- added J10: Config header (3x8), Connector_PinHeader_2.54mm:PinHeader_3x08_P2.54mm_Vertical, symbol z280s100:JP3x8
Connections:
- net +5V: now also J10.1 (HIGH), J10.10 (HIGH), J10.13 (HIGH), J10.16 (HIGH), J10.19 (HIGH), J10.22 (HIGH), J10.4 (HIGH), J10.7 (HIGH)
- net BTI_AD0: now also J10.2 (BTI_AD0)
- net BTI_AD1: now also J10.5 (BTI_AD1)
- net BTI_AD2: now also J10.8 (BTI_AD2)
- net BTI_AD3: now also J10.11 (BTI_AD3)
- net BTI_AD4: now also J10.14 (BTI_AD4)
- net BTI_AD5: now also J10.17 (BTI_AD5)
- net BTI_AD6: now also J10.20 (BTI_AD6)
- net BTI_AD7: now also J10.23 (BTI_AD7)
- net GND: now also J10.12 (LOW), J10.15 (LOW), J10.18 (LOW), J10.21 (LOW), J10.24 (LOW), J10.3 (LOW), J10.6 (LOW), J10.9 (LOW)
